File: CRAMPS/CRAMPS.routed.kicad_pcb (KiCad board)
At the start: 2 copper layers, 99.1 x 99.1 mm, 191 parts, among them M101 PCB_GREEN_RMC, M102 LOGO_OSHW, P101 SOCKET_6_LONG, P102 HEADER_2, P103 HEADER_2, P201 PT_2,5-2-5,0-H, P202 KK-2.54-4W, P203 KK-2.54-4W, P204 KK-2.54-4W, P205 KK-2.54-4W, P206 KK-2.54-4W, P207 KK-2.54-4W, P208 POLOLU_SOCKET, P209 POLOLU_SOCKET, P210 POLOLU_SOCKET, P211 POLOLU_SOCKET, P301 HEADER_2, P302 KK-2.54-2W, P303 HEADER_4X2, P304 HEADER_3X2, P305 HEADER_6, P401 PT_2,5-2-5,0-H, P402 PT_2,5-2-5,0-H, P403 PT_2,5-2-5,0-H, P404 PT_1,5-3-3,5-H, P405 PT_1,5-2-3,5-H, P406 PT_1,5-2-3,5-H, P407 KK-2.54-2W, P408 PT_1,5-2-3,5-H, P409 KK-2.54-2W, P501 HEADER_6, P502 HEADER_6X2, P503 HEADER_4X2, P504 HEADER_4X2, P8 BB_EXP_CONN, P9 BB_EXP_CONN, Q101 2N7002K, Q301 2N7002K, Q302 2N7002K, Q303 2N7002K, Q304 2N7002K, Q401 IRLB8743PBF, Q402 IRLB8743PBF, Q403 IRLB8743PBF, Q404 DMN2075U, Q405 IRLB8743PBF, Q406 DMN2075U, SW101 SW_PUSH, SW102 SW_PUSH, U201 Pololu, U202 Pololu, U203 Pololu, U204 Pololu, U205 Pololu, U206 Pololu, U301 24C256, U302 74ACT244, U501 74CBTD3861

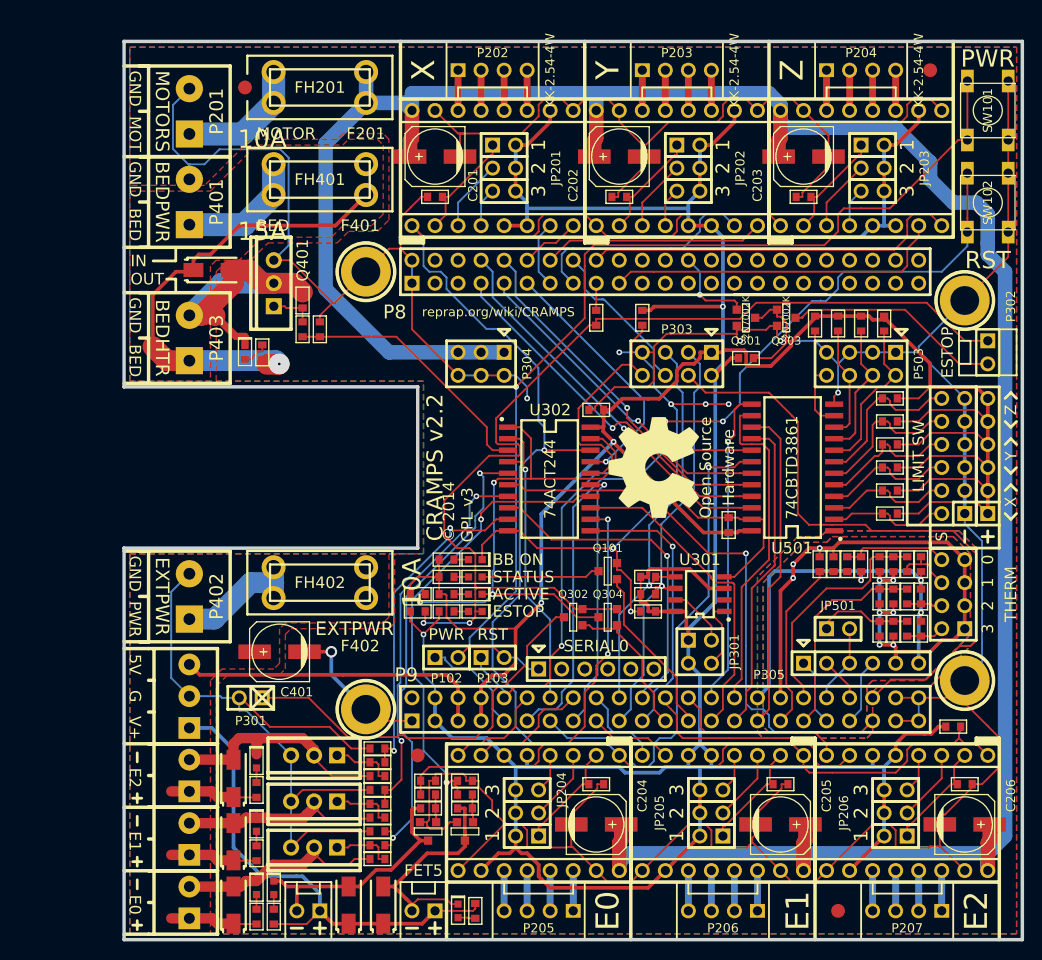
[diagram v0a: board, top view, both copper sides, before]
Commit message: Fix inverted ESTOP LED Requires adding one more 2N7002K
Signed-off-by: Charles Steinkuehler <charles@steinkuehler.net>
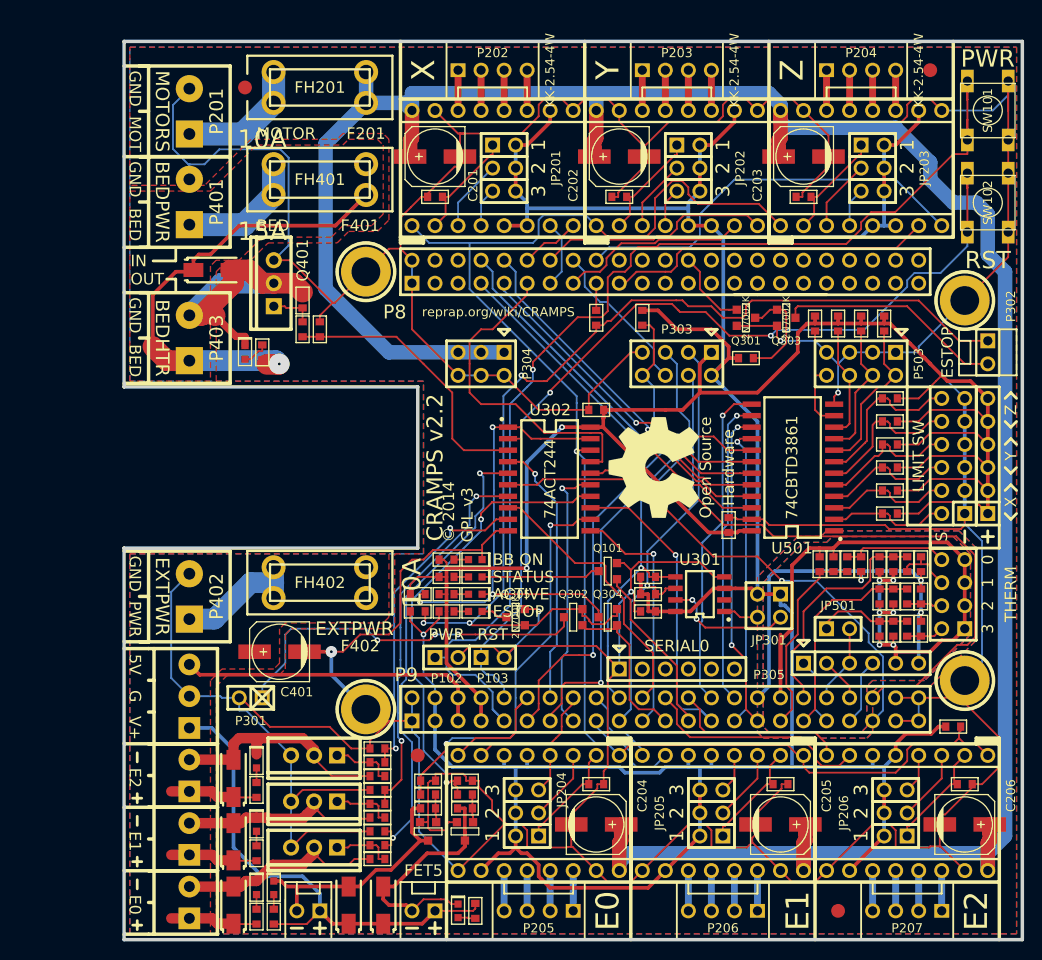
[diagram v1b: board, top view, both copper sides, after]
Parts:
- added Q305: 2N7002K, SOT23GDS, F.Cu at (94.0, 97.8)
- moved JP301 9.16 mm to (121.9, 96.5), turned to 180 degrees
- moved P101 8.89 mm to (111.8, 103.5)
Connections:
- net ESTOP_SWn renamed ESTOP_SW
- net ESTOPn renamed ESTOP
- LD302 pad K: N-00000183 -> N-00000185
- P302 pad 1: N-00000183 -> N-00000184
- Q302 pad S: N-00000183 -> N-00000184
- Q304 pad S: N-00000183 -> N-00000184
- R302 pad 1: N-00000183 -> N-00000184
- R304 pad 2: N-00000183 -> N-00000184
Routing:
- net N-00000183: track 118.2 -> 0.00 mm, vias 2 -> 0
- net N-00000184: track 0.00 -> 115.4 mm, vias 0 -> 3
- net DGND: track 644.1 -> 716.8 mm, vias 12 -> 5
- net E0_EN_BUFn: track 180.5 -> 165.2 mm
- net Z-MIN: track 55.6 -> 46.7 mm, vias 1 -> 2
- net /Emergency Stop/MACHINE_PWRn: track 62.7 -> 54.0 mm
- net FET1: track 28.5 -> 36.3 mm, vias 1 -> 0
- net N-00000180: track 6.74 -> 14.3 mm, vias 0 -> 2
- net PWR_BUT: track 117.8 -> 125.3 mm
- net RESETn: track 98.5 -> 104.9 mm, vias 3 -> 2
- net FET6: track 37.0 -> 30.6 mm, vias 1 -> 0
- net Y_STEP: track 25.9 -> 20.9 mm
- net FET5: track 62.5 -> 57.8 mm
- net +V_MOTOR: track 279.7 -> 284.2 mm
- net D3.3V: track 330.6 -> 334.8 mm, vias 2 -> 1
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
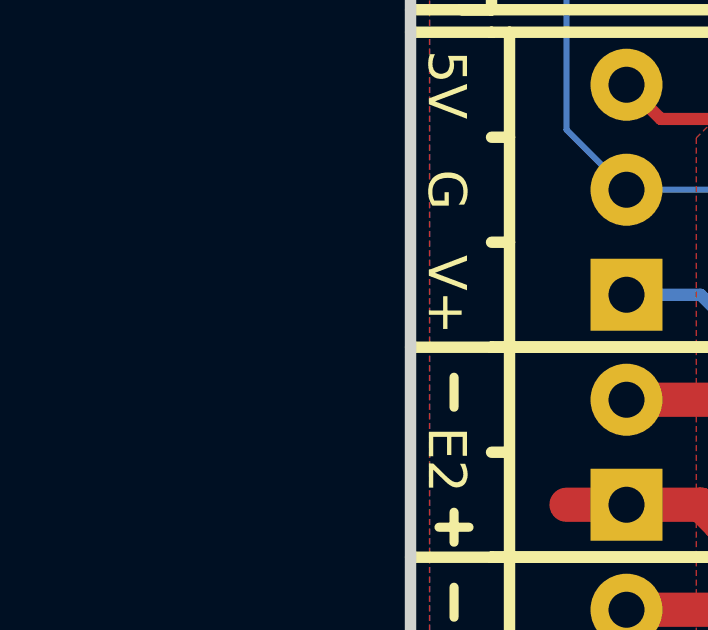
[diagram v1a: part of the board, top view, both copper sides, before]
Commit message: Switch to tape/reel part number for '244 buffer
Signed-off-by: Charles Steinkuehler <charles@steinkuehler.net>
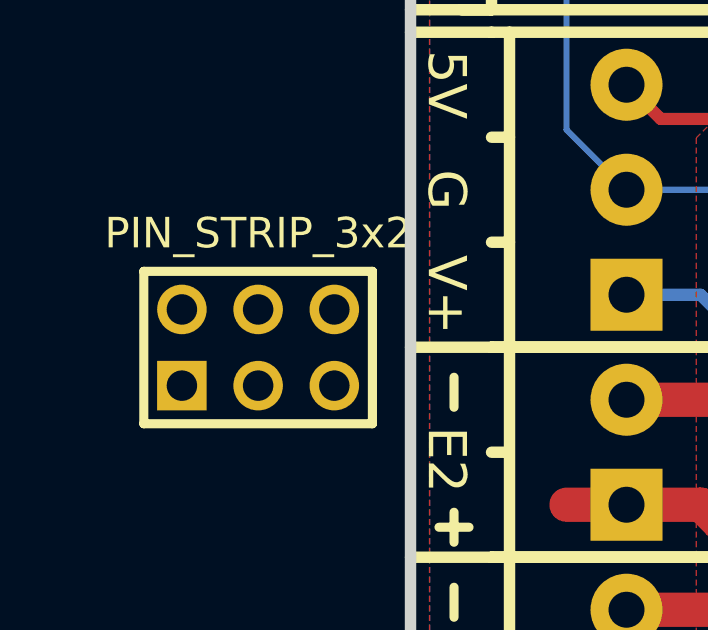
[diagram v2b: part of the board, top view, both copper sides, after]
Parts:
- added PIN_STRIP_3x2: Val**, pin_strip_3x2, F.Cu at (45.7, 111.8)
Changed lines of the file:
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@@
     (links 451)
     (no_connects 0)
-    (area 50.609499 34.099499 150.050501 133.540501)
+    (area 23.6982 8.84428 158.9278 149.3012)
     (thickness 1.6002)
     (drawings 291)
     (tracks 1823)
     (zones 0)
-    (modules 192)
+    (modules 193)
     (nets 156)
   )
@@
     (19 F.Paste user)
     (20 B.SilkS user)
-    (21 F.SilkS user hide)
+    (21 F.SilkS user)
     (22 B.Mask user)
     (23 F.Mask user)
@@
       (rotate (xyz 0 0 0))
     )
+  )
+  (module pin_strip_3x2 (layer Front)
+    (at 45.72 111.76)
+    (descr "Pin strip 4x2pin")
+    (tags "CONN DEV")
+    (path pin_strip_4x2)
+    (fp_text reference PIN_STRIP_3x2 (at 0 -3.81) (layer F.SilkS)
+      (effects (font (size 1.016 1.016) (thickness 0.2032)))
+    )
+    (fp_text value Val** (at 0 0) (layer F.SilkS) hide
+      (effects (font (size 1.016 0.889) (thickness 0.2032)))
+    )
+    (fp_line (start -3.81 -2.54) (end 3.81 -2.54) (layer F.SilkS) (width 0.3048))
+    (fp_line (start 3.81 -2.54) (end 3.81 2.54) (layer F.SilkS) (width 0.3048))
+    (fp_line (start 3.81 2.54) (end -3.81 2.54) (layer F.SilkS) (width 0.3048))
+    (fp_line (start -3.81 -2.54) (end -3.81 2.54) (layer F.SilkS) (width 0.3048))
+    (pad 1 thru_hole rect (at -2.54 1.27) (size 1.651 1.651) (drill 1.016)
+      (layers *.Cu *.Mask F.SilkS)
+    )
+    (pad 2 thru_hole circle (at -2.54 -1.27) (size 1.651 1.651) (drill 1.016)
+      (layers *.Cu *.Mask F.SilkS)
+    )
+    (pad 3 thru_hole circle (at 0 1.27) (size 1.651 1.651) (drill 1.016)
+      (layers *.Cu *.Mask F.SilkS)
+    )
+    (pad 4 thru_hole circle (at 0 -1.27) (size 1.651 1.651) (drill 1.016)
+      (layers *.Cu *.Mask F.SilkS)
+    )
+    (pad 5 thru_hole circle (at 2.54 1.27) (size 1.651 1.651) (drill 1.016)
+      (layers *.Cu *.Mask F.SilkS)
+    )
+    (pad 6 thru_hole circle (at 2.54 -1.27) (size 1.651 1.651) (drill 1.016)
+      (layers *.Cu *.Mask F.SilkS)
+    )
+    (model walter\pin_strip\pin_strip_4x2.wrl
+      (at (xyz 0 0 0))
+      (scale (xyz 1 1 1))
+      (rotate (xyz 0 0 0))
+    )

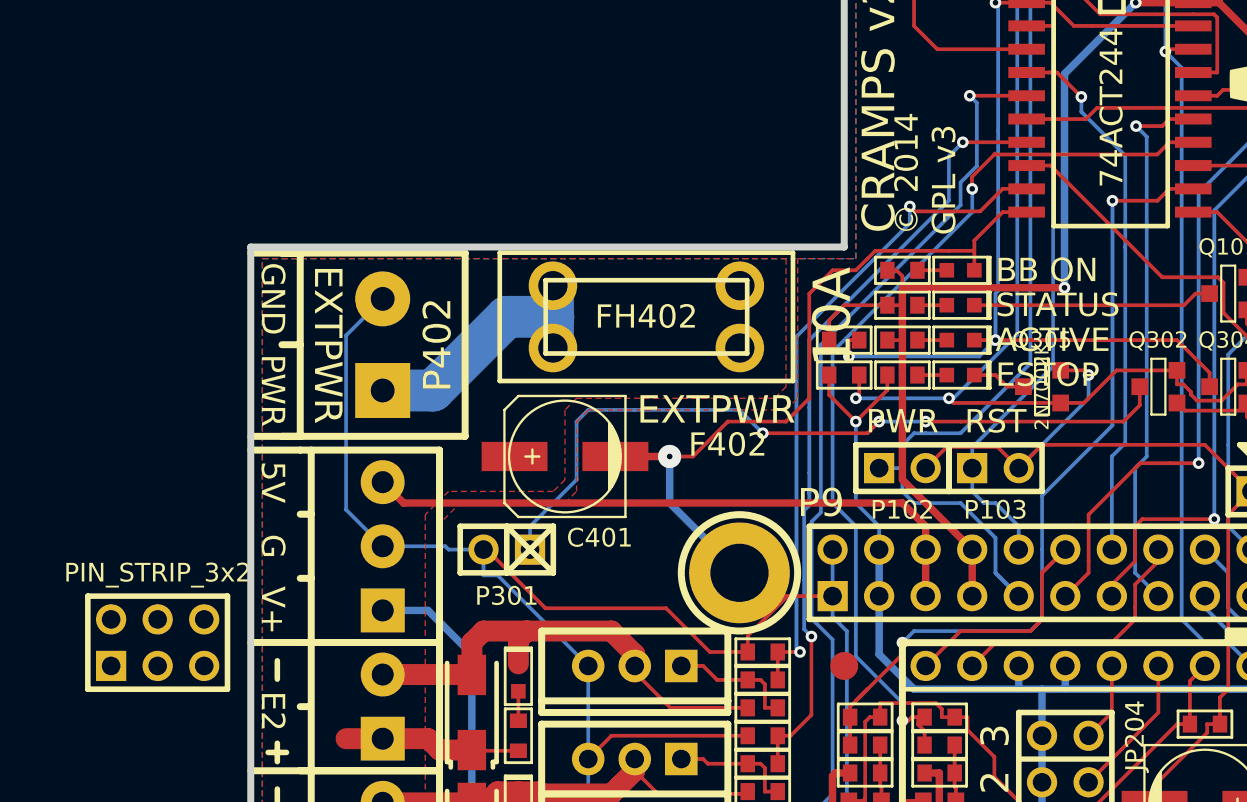
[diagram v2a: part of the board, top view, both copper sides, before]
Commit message: Delete temporary 3x2 pin header ...used as size reference for possibly adding back 3-pin header for 7805 style footprint for 5V switching regulator
Signed-off-by: Charles Steinkuehler <charles@steinkuehler.net>
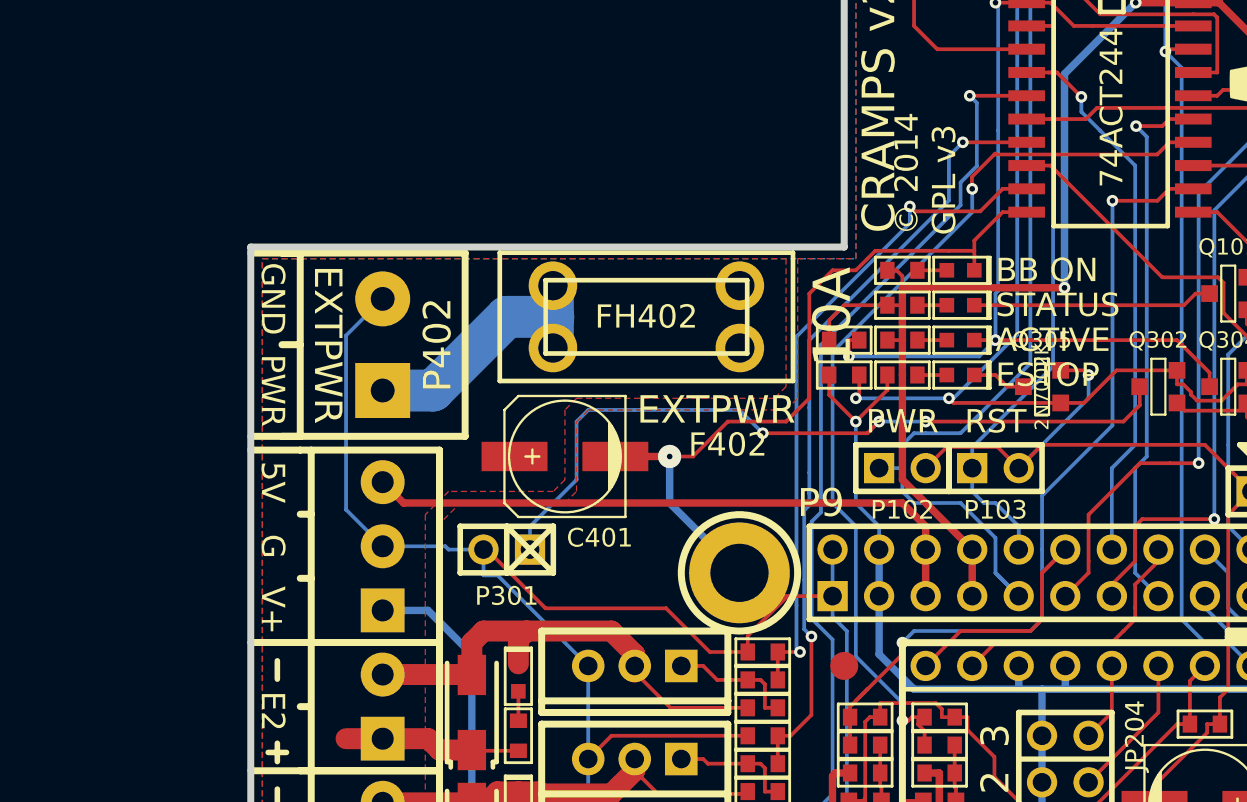
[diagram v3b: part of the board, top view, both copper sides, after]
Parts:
- removed PIN_STRIP_3x2: Val**, pin_strip_3x2
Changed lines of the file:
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@@
     (tracks 1823)
     (zones 0)
-    (modules 193)
+    (modules 192)
     (nets 156)
   )
@@
   (layers
     (15 Front signal)
-    (0 Back signal)
+    (0 Back signal hide)
     (16 B.Adhes user)
     (17 F.Adhes user)
@@
     )
   )
-  (module pin_strip_3x2 (layer Front)
-    (at 45.72 111.76)
-    (descr "Pin strip 4x2pin")
-    (tags "CONN DEV")
-    (path pin_strip_4x2)
-    (fp_text reference PIN_STRIP_3x2 (at 0 -3.81) (layer F.SilkS)
-      (effects (font (size 1.016 1.016) (thickness 0.2032)))
-    )
-    (fp_text value Val** (at 0 0) (layer F.SilkS) hide
-      (effects (font (size 1.016 0.889) (thickness 0.2032)))
-    )
-    (fp_line (start -3.81 -2.54) (end 3.81 -2.54) (layer F.SilkS) (width 0.3048))
-    (fp_line (start 3.81 -2.54) (end 3.81 2.54) (layer F.SilkS) (width 0.3048))
-    (fp_line (start 3.81 2.54) (end -3.81 2.54) (layer F.SilkS) (width 0.3048))
-    (fp_line (start -3.81 -2.54) (end -3.81 2.54) (layer F.SilkS) (width 0.3048))
-    (pad 1 thru_hole rect (at -2.54 1.27) (size 1.651 1.651) (drill 1.016)
-      (layers *.Cu *.Mask F.SilkS)
-    )
-    (pad 2 thru_hole circle (at -2.54 -1.27) (size 1.651 1.651) (drill 1.016)
-      (layers *.Cu *.Mask F.SilkS)
-    )
-    (pad 3 thru_hole circle (at 0 1.27) (size 1.651 1.651) (drill 1.016)
-      (layers *.Cu *.Mask F.SilkS)
-    )
-    (pad 4 thru_hole circle (at 0 -1.27) (size 1.651 1.651) (drill 1.016)
-      (layers *.Cu *.Mask F.SilkS)
-    )
-    (pad 5 thru_hole circle (at 2.54 1.27) (size 1.651 1.651) (drill 1.016)
-      (layers *.Cu *.Mask F.SilkS)
-    )
-    (pad 6 thru_hole circle (at 2.54 -1.27) (size 1.651 1.651) (drill 1.016)
-      (layers *.Cu *.Mask F.SilkS)
-    )
-    (model walter\pin_strip\pin_strip_4x2.wrl
-      (at (xyz 0 0 0))
-      (scale (xyz 1 1 1))
-      (rotate (xyz 0 0 0))
-    )
-  )
   (gr_line (start 86.36 133.35) (end 86.36 127) (angle 90) (layer F.SilkS) (width 0.381))
   (gr_line (start 106.68 133.35) (end 106.68 127) (angle 90) (layer F.SilkS) (width 0.381))
@@
   (segment (start 130.81 102.87) (end 128.27 105.41) (width 0.2032) (layer Back) (net 49))
   (segment (start 130.81 102.87) (end 130.81 99.06) (width 0.2032) (layer Front) (net 49))
+  (segment (start 97.155 83.82) (end 99.06 85.725) (width 0.2032) (layer Back) (net 50))
+  (segment (start 99.06 100.965) (end 97.79 102.235) (width 0.2032) (layer Back) (net 50))
+  (segment (start 99.06 85.725) (end 99.06 100.965) (width 0.2032) (layer Back) (net 50))
   (segment (start 94.615 80.645) (end 94.615 78.105) (width 0.2032) (layer Front) (net 50))
   (segment (start 94.615 78.105) (end 93.14 78.105) (width 0.2032) (layer Front) (net 50))
   (segment (start 96.1261 81.9752) (end 96.1261 82.7911) (width 0.2032) (layer Back) (net 50))
-  (segment (start 96.1261 82.7911) (end 98.52 85.185) (width 0.2032) (layer Back) (net 50))
-  (segment (start 98.52 90.17) (end 98.52 100.87) (width 0.2032) (layer Back) (net 50))
-  (segment (start 98.52 90.17) (end 98.52 85.185) (width 0.2032) (layer Back) (net 50))
-  (segment (start 98.52 100.87) (end 97.79 101.6) (width 0.2032) (layer Back) (net 50))
-  (segment (start 97.79 101.6) (end 97.79 106.68) (width 0.2032) (layer Back) (net 50))
+  (segment (start 96.1261 82.7911) (end 97.155 83.82) (width 0.2032) (layer Back) (net 50))
+  (segment (start 97.79 102.235) (end 97.79 106.68) (width 0.2032) (layer Back) (net 50))
   (via (at 96.1261 81.9752) (size 0.635) (layers Front Back) (net 50))
   (segment (start 93.14 80.645) (end 94.3434 80.645) (width 0.2032) (layer Front) (net 50))

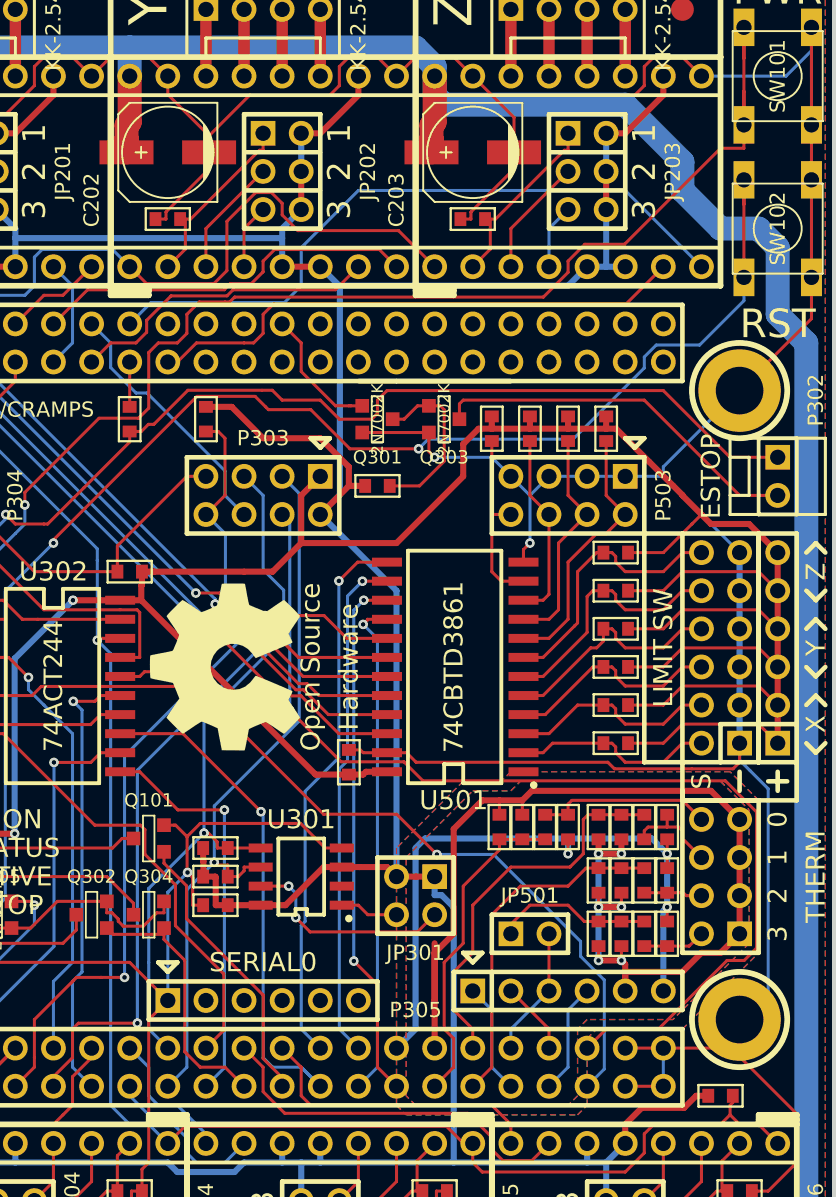
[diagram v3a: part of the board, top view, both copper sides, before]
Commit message: Continued post-autorouter PCB cleanup
Signed-off-by: Charles Steinkuehler <charles@steinkuehler.net>
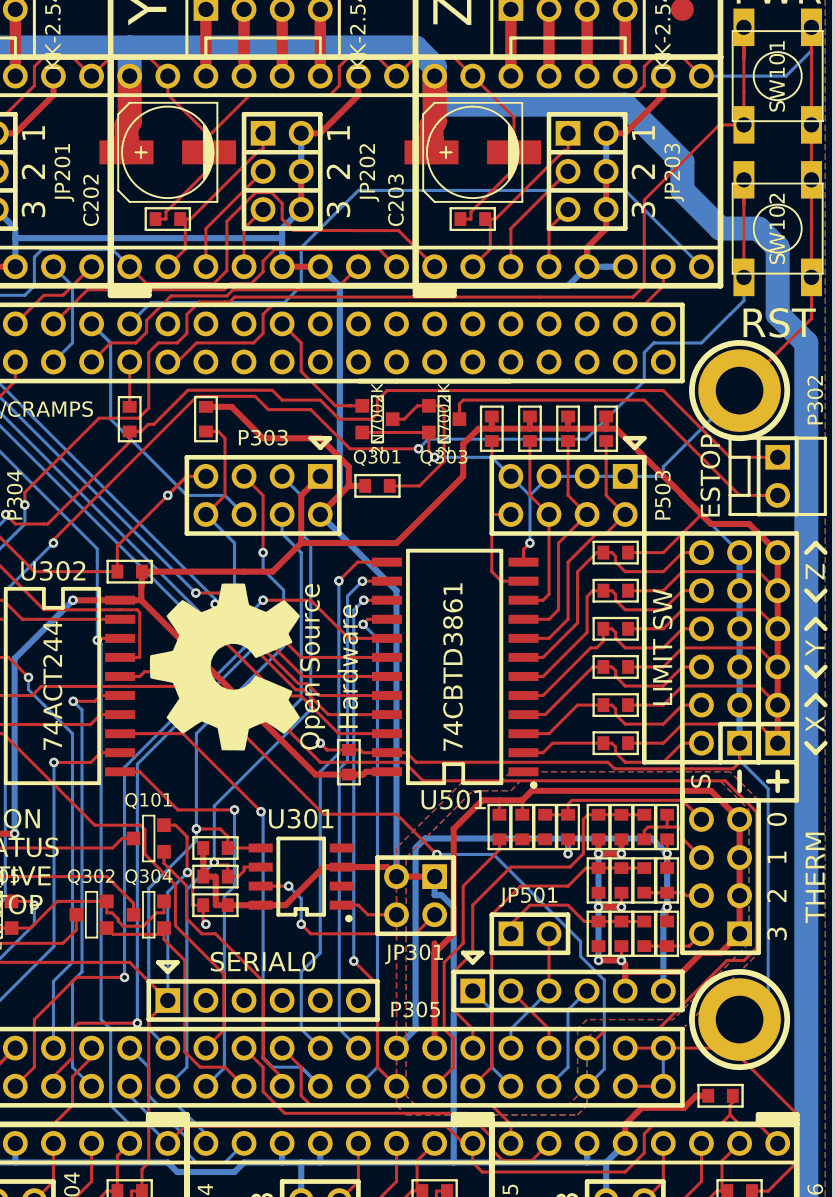
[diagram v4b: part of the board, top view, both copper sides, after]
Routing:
- net DGND: track 716.8 -> 710.7 mm, vias 5 -> 8
- net Z-MIN: track 46.7 -> 49.8 mm
- net SPI_SPARE: track 17.3 -> 20.2 mm
- net Z-MAX: track 48.9 -> 50.4 mm
- net SPI_CS1: track 70.3 -> 71.8 mm
- net FET4: track 26.9 -> 27.9 mm
- net EN_CRAMP3n: track 23.6 -> 24.4 mm
- net SDA: track 47.9 -> 48.7 mm, vias 1 -> 2
- net Z_STEP: track 36.4 -> 37.1 mm
- net RESETn: track 104.9 -> 105.6 mm
- net SCL: track 49.1 -> 49.7 mm
- net LED: track 18.9 -> 19.4 mm
- net D3.3V: track 334.8 -> 335.4 mm
